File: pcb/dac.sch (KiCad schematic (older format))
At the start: 65 parts, among them U6 MAX5853ETL-T, U7 TLV3542IDR

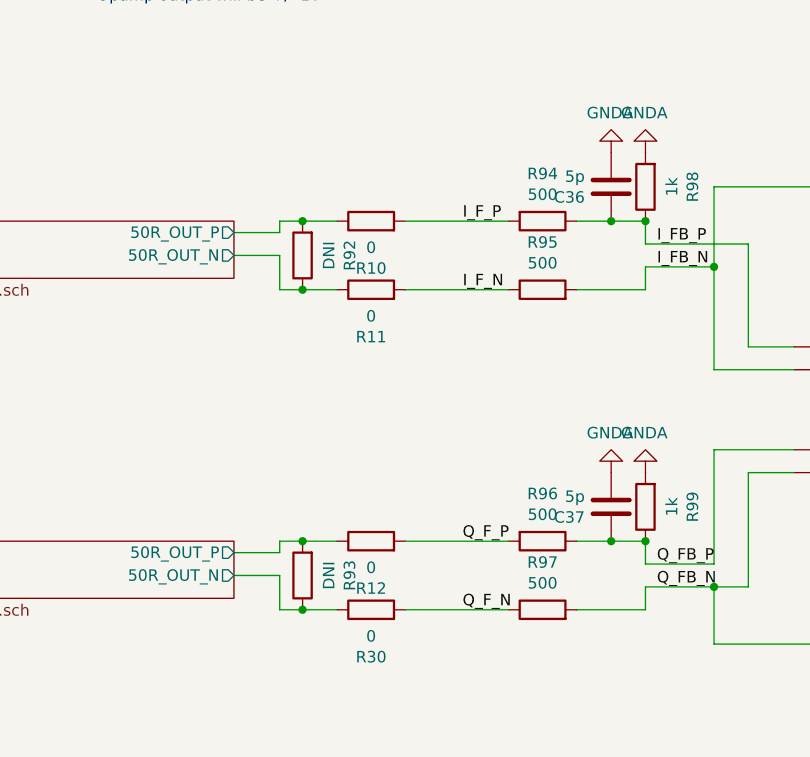
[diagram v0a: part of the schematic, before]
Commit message: clean up baseband amplifier routing, make it like the LO amp
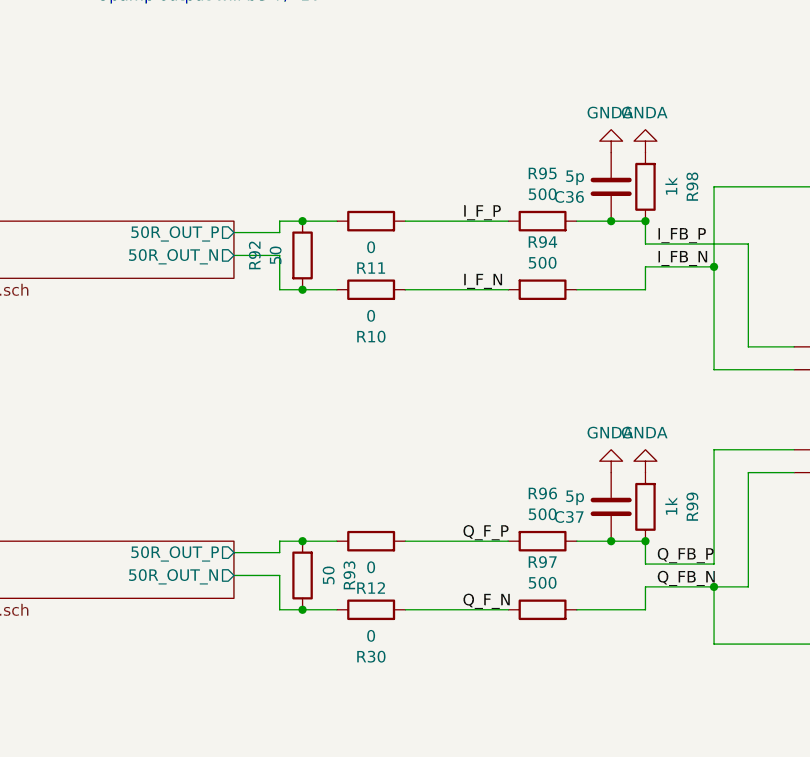
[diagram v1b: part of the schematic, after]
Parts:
- R92, R93: value DNI -> 50
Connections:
- net I AA Filter/50R_OUT_N: now also R10.1, R92.2; no longer R11.1, R92.1
- net I AA Filter/50R_OUT_P: now also R11.1, R92.1; no longer R10.1, R92.2
- net I_FB_N: now also R94.1; no longer R95.2
- net I_FB_P: now also R95.2; no longer R94.1
- net I_F_N: now also R10.2, R94.2; no longer R11.2, R95.1
- net I_F_P: now also R11.2, R95.1; no longer R10.2, R94.2
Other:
- moved on the sheet: R10, R11, R94, R95
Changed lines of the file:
@@
 L Device:R R95
 U 1 1 5FB7ADB0
-P 5050 5050
-F 0 "R95" V 5257 5050 50  0000 C CNN
-F 1 "500" V 5166 5050 50  0000 C CNN
-F 2 "Resistor_SMD:R_0603_1608Metric" V 4980 5050 50  0001 C CNN
-F 3 "~" H 5050 5050 50  0001 C CNN
-	1    5050 5050
-	0    -1   -1   0
-$EndComp
-$Comp
-L Device:R R94
-U 1 1 5FB7ADB6
 P 5050 4750
-F 0 "R94" V 4843 4750 50  0000 C CNN
-F 1 "500" V 4934 4750 50  0000 C CNN
+F 0 "R95" V 5257 4750 50  0000 C CNN
+F 1 "500" V 5166 4750 50  0000 C CNN
 F 2 "Resistor_SMD:R_0603_1608Metric" V 4980 4750 50  0001 C CNN
 F 3 "~" H 5050 4750 50  0001 C CNN
 	1    5050 4750
-	0    1    1    0
+	0    -1   -1   0
 $EndComp
 Connection ~ 1150 4750
@@
 P 4000 4900
 F 0 "R92" V 3793 4900 50  0000 C CNN
-F 1 "DNI" V 3884 4900 50  0000 C CNN
+F 1 "50" V 3884 4900 50  0000 C CNN
 F 2 "Resistor_SMD:R_0603_1608Metric" V 3930 4900 50  0001 C CNN
 F 3 "~" H 4000 4900 50  0001 C CNN
 	1    4000 4900
-	-1   0    0    1
+	1    0    0    -1
 $EndComp
 $Comp
@@
 P 4000 6300
 F 0 "R93" V 3793 6300 50  0000 C CNN
-F 1 "DNI" V 3884 6300 50  0000 C CNN
+F 1 "50" V 3884 6300 50  0000 C CNN
 F 2 "Resistor_SMD:R_0603_1608Metric" V 3930 6300 50  0001 C CNN
 F 3 "~" H 4000 6300 50  0001 C CNN
@@
 Wire Wire Line
 	3900 4800 3900 4750
-Wire Wire Line
-	3700 4900 3900 4900
 Wire Wire Line
 	3900 4900 3900 5050
@@
 Wire Wire Line
 	4000 6150 3900 6150
-Connection ~ 4000 5050
-Wire Wire Line
-	4000 5050 3900 5050
-Connection ~ 4000 4750
-Wire Wire Line
-	4000 4750 3900 4750
 $Comp
 L Device:R R104
@@
 L Device:R R10
 U 1 1 5FD72039
+P 4300 5050
+F 0 "R10" V 4093 5050 50  0000 C CNN
+F 1 "0" V 4184 5050 50  0000 C CNN
+F 2 "Resistor_SMD:R_0603_1608Metric" V 4230 5050 50  0001 C CNN
+F 3 "~" H 4300 5050 50  0001 C CNN
+	1    4300 5050
+	0    -1   -1   0
+$EndComp
+Wire Wire Line
+	4450 4750 4900 4750
+$Comp
+L Device:R R11
+U 1 1 5FD85387
 P 4300 4750
-F 0 "R10" V 4093 4750 50  0000 C CNN
+F 0 "R11" V 4093 4750 50  0000 C CNN
 F 1 "0" V 4184 4750 50  0000 C CNN
 F 2 "Resistor_SMD:R_0603_1608Metric" V 4230 4750 50  0001 C CNN
@@
 	0    -1   -1   0
 $EndComp
-Wire Wire Line
-	4000 4750 4150 4750
-Wire Wire Line
-	4450 4750 4900 4750
-$Comp
-L Device:R R11
-U 1 1 5FD85387
-P 4300 5050
-F 0 "R11" V 4093 5050 50  0000 C CNN
-F 1 "0" V 4184 5050 50  0000 C CNN
-F 2 "Resistor_SMD:R_0603_1608Metric" V 4230 5050 50  0001 C CNN
-F 3 "~" H 4300 5050 50  0001 C CNN
-	1    4300 5050
-	0    -1   -1   0
-$EndComp
-Wire Wire Line
-	4000 5050 4150 5050
 Wire Wire Line
 	4450 5050 4900 5050
@@
 Wire Wire Line
 	8850 900  9400 900
+$Comp
+L Device:R R94
+U 1 1 5FB7ADB6
+P 5050 5050
+F 0 "R94" V 4843 5050 50  0000 C CNN
+F 1 "500" V 4934 5050 50  0000 C CNN
+F 2 "Resistor_SMD:R_0603_1608Metric" V 4980 5050 50  0001 C CNN
+F 3 "~" H 5050 5050 50  0001 C CNN
+	1    5050 5050
+	0    1    1    0
+$EndComp
+Wire Wire Line
+	3900 5050 4000 5050
+Wire Wire Line
+	3900 4750 4000 4750
+Connection ~ 4000 4750
+Wire Wire Line
+	4000 4750 4150 4750
+Connection ~ 4000 5050
+Wire Wire Line
+	4000 5050 4150 5050
+Wire Wire Line
+	3700 4900 3900 4900
 Wire Bus Line
 	5450 3350 5450 3600

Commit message: routing the dac wires
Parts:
- TP51, TP52, TP53, TP56, TP57, TP58: footprint TestPoint:TestPoint_Pad_D1.5mm -> TestPoint:TestPoint_Pad_D1.0mm
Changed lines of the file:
@@
 F 0 "TP56" H 10608 1018 50  0000 L CNN
 F 1 "TestPoint" H 10608 927 50  0000 L CNN
-F 2 "TestPoint:TestPoint_Pad_D1.5mm" H 10750 900 50  0001 C CNN
+F 2 "TestPoint:TestPoint_Pad_D1.0mm" H 10750 900 50  0001 C CNN
 F 3 "~" H 10750 900 50  0001 C CNN
 	1    10550 900
@@
 F 0 "TP57" H 10608 1868 50  0000 L CNN
 F 1 "TestPoint" H 10608 1777 50  0000 L CNN
-F 2 "TestPoint:TestPoint_Pad_D1.5mm" H 10750 1750 50  0001 C CNN
+F 2 "TestPoint:TestPoint_Pad_D1.0mm" H 10750 1750 50  0001 C CNN
 F 3 "~" H 10750 1750 50  0001 C CNN
 	1    10550 1750
@@
 F 0 "TP58" H 10608 2718 50  0000 L CNN
 F 1 "TestPoint" H 10608 2627 50  0000 L CNN
-F 2 "TestPoint:TestPoint_Pad_D1.5mm" H 10750 2600 50  0001 C CNN
+F 2 "TestPoint:TestPoint_Pad_D1.0mm" H 10750 2600 50  0001 C CNN
 F 3 "~" H 10750 2600 50  0001 C CNN
 	1    10550 2600
@@
 F 0 "TP52" H 6158 2368 50  0000 L CNN
 F 1 "TestPoint" H 6158 2277 50  0000 L CNN
-F 2 "TestPoint:TestPoint_Pad_D1.5mm" H 6300 2250 50  0001 C CNN
+F 2 "TestPoint:TestPoint_Pad_D1.0mm" H 6300 2250 50  0001 C CNN
 F 3 "~" H 6300 2250 50  0001 C CNN
 	1    6100 2250
@@
 F 0 "TP51" H 5758 2468 50  0000 L CNN
 F 1 "TestPoint" H 5758 2377 50  0000 L CNN
-F 2 "TestPoint:TestPoint_Pad_D1.5mm" H 5900 2350 50  0001 C CNN
+F 2 "TestPoint:TestPoint_Pad_D1.0mm" H 5900 2350 50  0001 C CNN
 F 3 "~" H 5900 2350 50  0001 C CNN
 	1    5700 2350
@@
 F 0 "TP53" H 6158 2768 50  0000 L CNN
 F 1 "TestPoint" H 6158 2677 50  0000 L CNN
-F 2 "TestPoint:TestPoint_Pad_D1.5mm" H 6300 2650 50  0001 C CNN
+F 2 "TestPoint:TestPoint_Pad_D1.0mm" H 6300 2650 50  0001 C CNN
 F 3 "~" H 6300 2650 50  0001 C CNN
 	1    6100 2650

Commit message: laying out split gnd pours
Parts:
- U6: footprint Package_DFN_QFN:QFN-40-1EP_6x6mm_P0.5mm_EP4.6x4.6mm_ThermalVias -> iq_siggen:qfn_max5853
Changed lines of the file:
@@
 F 0 "U6" H 3950 1715 50  0000 C CNN
 F 1 "MAX5853ETL-T" H 3950 1624 50  0000 C CNN
-F 2 "Package_DFN_QFN:QFN-40-1EP_6x6mm_P0.5mm_EP4.6x4.6mm_ThermalVias" H 2550 1350 50  0001 L BNN
+F 2 "iq_siggen:qfn_max5853" H 2550 1350 50  0001 L BNN
 F 3 "max5853etlt" H 2550 1350 50  0001 L BNN
 F 4 "MAXIM" H 2550 1350 50  0001 L BNN "Field4"

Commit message: routing contiued, add swtiches, remove test points, all parts now positioned on board
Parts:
- added TP4: TestPoint, TestPoint:TestPoint_Pad_D1.5mm, symbol Connector:TestPoint
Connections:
- net A_IOUT_N: now also R88.1; no longer R89.1
- net A_IOUT_P: now also R89.1; no longer R88.1
- net GNDS: now also TP4.1
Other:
- moved on the sheet: R88, R89
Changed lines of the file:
@@
 $Descr A4 11693 8268
 encoding utf-8
-Sheet 4 7
+Sheet 4 6
 Title ""
 Date ""
@@
 L Device:R R89
 U 1 1 5FB7ADA1
+P 1150 4600
+F 0 "R89" V 1357 4600 50  0000 C CNN
+F 1 "25" V 1266 4600 50  0000 C CNN
+F 2 "Resistor_SMD:R_0603_1608Metric" V 1080 4600 50  0001 C CNN
+F 3 "~" H 1150 4600 50  0001 C CNN
+	1    1150 4600
+	-1   0    0    1
+$EndComp
+$Comp
+L Device:R R88
+U 1 1 5FB7ADA7
 P 1150 5200
-F 0 "R89" V 1357 5200 50  0000 C CNN
-F 1 "25" V 1266 5200 50  0000 C CNN
+F 0 "R88" V 943 5200 50  0000 C CNN
+F 1 "25" V 1034 5200 50  0000 C CNN
 F 2 "Resistor_SMD:R_0603_1608Metric" V 1080 5200 50  0001 C CNN
 F 3 "~" H 1150 5200 50  0001 C CNN
 	1    1150 5200
 	1    0    0    -1
-$EndComp
-$Comp
-L Device:R R88
-U 1 1 5FB7ADA7
-P 1150 4600
-F 0 "R88" V 943 4600 50  0000 C CNN
-F 1 "25" V 1034 4600 50  0000 C CNN
-F 2 "Resistor_SMD:R_0603_1608Metric" V 1080 4600 50  0001 C CNN
-F 3 "~" H 1150 4600 50  0001 C CNN
-	1    1150 4600
-	-1   0    0    1
 $EndComp
 $Comp
@@
 $EndComp
 Wire Wire Line
-	1150 4750 1550 4750
-Wire Wire Line
 	1850 4750 2100 4750
 $Comp
@@
 Wire Wire Line
 	3700 4900 3900 4900
+Wire Wire Line
+	1150 4750 1550 4750
+$Comp
+L power:GNDS #PWR?
+U 1 1 5FDD9780
+P 11000 2100
+AR Path="/5FDD9780" Ref="#PWR?"  Part="1"
+AR Path="/5FB3742F/5FDD9780" Ref="#PWR0112"  Part="1"
+F 0 "#PWR0112" H 11000 1850 50  0001 C CNN
+F 1 "GNDS" H 11005 1927 50  0000 C CNN
+F 2 "" H 11000 2100 50  0001 C CNN
+F 3 "" H 11000 2100 50  0001 C CNN
+	1    11000 2100
+	1    0    0    -1
+$EndComp
+Wire Wire Line
+	11000 2100 10900 2100
+$Comp
+L Connector:TestPoint TP?
+U 1 1 5FDD9787
+P 10900 2100
+AR Path="/5FDD9787" Ref="TP?"  Part="1"
+AR Path="/5FB3742F/5FDD9787" Ref="TP4"  Part="1"
+F 0 "TP4" H 10842 2126 50  0000 R CNN
+F 1 "TestPoint" H 10842 2217 50  0000 R CNN
+F 2 "TestPoint:TestPoint_Pad_D1.5mm" H 11100 2100 50  0001 C CNN
+F 3 "~" H 11100 2100 50  0001 C CNN
+	1    10900 2100
+	1    0    0    -1
+$EndComp
+$Comp
+L power:PWR_FLAG #FLG?
+U 1 1 5FDD978D
+P 11000 2100
+AR Path="/5FDD978D" Ref="#FLG?"  Part="1"
+AR Path="/5FB3742F/5FDD978D" Ref="#FLG0101"  Part="1"
+F 0 "#FLG0101" H 11000 2175 50  0001 C CNN
+F 1 "PWR_FLAG" H 11000 2273 50  0000 C CNN
+F 2 "" H 11000 2100 50  0001 C CNN
+F 3 "~" H 11000 2100 50  0001 C CNN
+	1    11000 2100
+	1    0    0    -1
+$EndComp
+Connection ~ 11000 2100
 Wire Bus Line
 	5450 3350 5450 3600

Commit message: layout refininements, stitching vias
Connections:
- net GNDD is gone; now on net GNDA: C55.2, C58.2, C63.2, U6.17 (DGND)
- net GNDS is gone; now on net GNDA: C49.2, C54.2, C57.2, C62.2, R100.1, TP4.1, U6.24 (*DCE), U6.29 (CGND)
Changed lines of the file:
@@
 $EndComp
 Connection ~ 11000 2100
+$Comp
+L power:GNDD #PWR?
+U 1 1 5FD41563
+P 8850 3200
+AR Path="/5FD41563" Ref="#PWR?"  Part="1"
+AR Path="/5FB3742F/5FD41563" Ref="#PWR?"  Part="1"
+F 0 "#PWR?" H 8850 2950 50  0001 C CNN
+F 1 "GNDD" H 8854 3045 50  0000 C CNN
+F 2 "" H 8850 3200 50  0001 C CNN
+F 3 "" H 8850 3200 50  0001 C CNN
+	1    8850 3200
+	1    0    0    -1
+$EndComp
+$Comp
+L power:GNDS #PWR?
+U 1 1 5FD41757
+P 9050 3200
+AR Path="/5FD41757" Ref="#PWR?"  Part="1"
+AR Path="/5FB3742F/5FD41757" Ref="#PWR?"  Part="1"
+F 0 "#PWR?" H 9050 2950 50  0001 C CNN
+F 1 "GNDS" H 9055 3027 50  0000 C CNN
+F 2 "" H 9050 3200 50  0001 C CNN
+F 3 "" H 9050 3200 50  0001 C CNN
+	1    9050 3200
+	1    0    0    -1
+$EndComp
+$Comp
+L power:GNDA #PWR?
+U 1 1 5FD41A7F
+P 8700 3200
+AR Path="/5FD41A7F" Ref="#PWR?"  Part="1"
+AR Path="/5FB3742F/5FD41A7F" Ref="#PWR?"  Part="1"
+F 0 "#PWR?" H 8700 2950 50  0001 C CNN
+F 1 "GNDA" H 8705 3027 50  0000 C CNN
+F 2 "" H 8700 3200 50  0001 C CNN
+F 3 "" H 8700 3200 50  0001 C CNN
+	1    8700 3200
+	1    0    0    -1
+$EndComp
+Wire Wire Line
+	8700 3200 8850 3200
 Wire Bus Line
 	5450 3350 5450 3600
@@
 Wire Bus Line
 	2450 1250 2450 2150
+Connection ~ 8850 3200
+Wire Wire Line
+	8850 3200 9050 3200
 $EndSCHEMATC

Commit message: populate LCSC BOM for JLCPCB assembly
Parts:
- C36, C37, C39, C40: value 5p -> 4.7p; LCSC (none) -> C1669
- C38, C41, C42, C43, C44, C48, C49, C51, C52, C53, C54, C55, C56, C57, C58: LCSC (none) -> C14663
- C59, C60, C61, C62, C63, C64, C65: LCSC (none) -> C19702
- FB3, FB4, FB5, FB6, FB7: LCSC (none) -> C19330
- R10, R11, R12, R2, R3, R30, R4, R5: LCSC (none) -> C21189
- R102, R103, R98, R99: LCSC (none) -> C21190
- R104, R105, R92, R93: value 50 -> 49.9; LCSC (none) -> C23185
- R88, R89, R90, R91: value 25 -> 24.9; LCSC (none) -> C22916
- R94, R95, R96, R97: value 500 -> 499; LCSC (none) -> C23065
